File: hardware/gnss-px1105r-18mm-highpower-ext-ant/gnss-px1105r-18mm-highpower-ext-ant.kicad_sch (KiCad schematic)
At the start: 28 parts, among them J4 BM05B-SRSS-TB, J9 2337019-1, U1 PX1105R, U3 TPS62913RPUR

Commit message: hardware: battery protection, boost swap, and a capacitor voltage audit
Base station power chain, all verified against exported netlists:

- Protection: MAX17303G+ gauge/protector and its NTMD6N02R2G FET pair
  replaced by DW01A + 2x FS8205A. The MAX17303 had no firmware driver and
  the board never had a working coulomb counter, so state of charge already
  came from the voltage curve in bs_battery_soc.h; it now reads a 1M/1M
  divider on GPIO1. The FETs move from the positive rail to the negative
  one because the DW01A has no charge pump, so board ground is now P-,
  separated from the cell's B- by the FET stack. Two FS8205A in parallel
  put the 150 mV overcurrent trip at ~4.8-6.0 A instead of ~2.4-3.0 A.
  TH1 moves onto the BQ21040's TS pin, replacing a fixed 10k that had been
  defeating thermal charge cutoff.

- V_LORA retargeted 7.49 V -> 4.95 V and LM5157QRTERQ1 -> TPS61023DRLR.
  Nothing needed 7.4 V (everything downstream is 3.3 V behind the
  TPS62913), while an RFD868x-class radio is 5 V nominal with a 6 V
  absolute maximum, so the old rail put it permanently out of reach. Being
  synchronous and internally compensated also dropped D2, C35-C38 and R10.
  Inductor stays the fleet 2.2 uH: inside TI's 0.37-2.9 uH range and the
  only value meeting their ripple-under-40%-of-average guidance at load.

- Keystone 1043P holder -> MYOUNG BH-18650-A5BJ001-2D. Terminal pitch
  72.30 vs 72.22 mm, so the battery nets did not move; BT2 is rotated 180
  degrees because this part's positive end is mirrored.

Across all four boards:

- Every crystal was mis-loaded. 32.768 kHz parts saw ~9 pF against a 6 pF
  spec and the 40 MHz saw 12.5 pF against 10 pF, both pulling slow. Moved
  to Seiko SC-32S (12.5 pF) with 22 pF load caps, and the 40 MHz caps to
  18 pF. The tolerance being paid for had been swamped several times over.

- Capacitor voltage audit, new Min V rating column in the BOM. Three parts
  were operating outside their rating on 8.4 V rails: 47 uF and 100 u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
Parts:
- J4: footprint CONN_BM05B-SRSS-TB_JST -> Footprints:CONN_BM05B-SRSS-TB_JST
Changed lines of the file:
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@@
 			)
 		)
-		(property "Footprint" "CONN_BM05B-SRSS-TB_JST"
+		(property "Footprint" "Footprints:CONN_BM05B-SRSS-TB_JST"
 			(at 233.045 80.645 0)
 			(hide yes)

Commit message: hardware: declare filled+capped vias on the 6-layer boards; in-progress board edits
Two separate things, kept together because they land in the same board files.

1. Via protection, mine.  lora-daughterboard and rocket-computer both place
   vias in pads, and the fab fills those on 6-layer stackups -- but the board
   files still declared (filling no) (capping no), so nothing in the exported
   data said so.  Both now declare IPC-4761 Type VII (filled and capped),
   which is the process via-in-pad actually requires.  base-station is left at
   (filling no) (capping no): it is 4-layer and does not get the treatment.

2. In-progress layout work, the user's, carried along in the same files:

   rocket-computer  J7 removed (superseded by the J8 JST VH battery inlet);
                    C20/C22/C48/C49 crystal caps 18 pF -> 12 pF now reflected
                    in copper; 8 parts flipped side, 23 repositioned, routing
                    and via count adjusted to suit
   lora-daughterboard  routing and ground stitching (+8 vias, +10 segments)
   base-station     one via removed
   gnss-sam10m8-18mm-hv       C15 added; C11/C13 47 uF -> 22 uF
   gnss-px1105r-...-ext-ant   C16/R8/R9 added; C13/C14 47 uF -> 22 uF

The 47 -> 22 uF swap on both GNSS boards is already reflected in the
cross-board BOM: the 47 uF line is now rocket-computer only (1), and 22 uF
GNSS went 5 -> 8.

Co-Authored-By: Claude Opus 5 <noreply@anthropic.com>
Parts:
- added C16: 22 uF, Capacitor_SMD:C_0805_2012Metric, symbol Device:C
- added R8, R9: 1 k, Resistor_SMD:R_0402_1005Metric, symbol Device:R_US
- C13, C14: value 47 uF -> 22 uF
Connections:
- net GND: now also C16.2
- net GNSS_RX: now also R9.1; no longer J4.1
- net GNSS_TX: now also R8.1; no longer J4.2
- net at C13.1, C14.1, FB1.1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: now also C16.1
- new net: J4.1, R9.2
- new net: J4.2, R8.2

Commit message: hardware: SMF10A TVS on VSYS -- LoRa CR5 and both GNSS boards (schematics)
Closes the LoRa review's finding 12, and extends it to the two GNSS
daughterboards, which turned out to have the same gap in a worse form.

VSYS is fed straight from an externally-handled connector that hot-plugs onto a
live 2S pack, and clamps nothing before the TPS62913's 18 V VIN abs max:

  lora  VSYS = { CR1.1, CR3.1, FL1.1 }   an ORing Schottky damps the ring
  gnss  VSYS = { FL1.1, J.3 }            connector pin straight into the choke

The GNSS boards lack the one element that was damping the LoRa board, so they
sit closer to the limit -- ~14.4 V worst-case ring against ~12.6 V. Neither
breaches 18 V on the hot-plug transient alone; the argument for the part is ESD
on a human-handled connector whose power pin has no protection, while the USB
port beside it does.

Part: PTTC SMF10A, LCSC C5444308, 56k in stock, $0.086 at 50+.
V_RWM 10 V is 19% above the 8.4 V full-charge pack, and V_BR 11.1 V min stays
clear of it even at -40 C. V_C 17 V at 11.8 A sits under the 18 V abs max --
that is what selects this part. The next step up, SMF12A, clamps at 19.9 V,
ABOVE the abs max, so it would pass through the very event being clamped. 10 V
is the only SMF step that clears both ends of this rail's narrow window.

Symbol/footprint/3D were already in the project, unused, from the SS24FL line
that was never fitted -- same SOD-123FL package, pads named A/C. New
Custom:SMF10A reuses Footprints:SODFL3617X108N and 3dmodels/SS24FL.step, with a
zener-style cathode bar so it reads as a unidirectional TVS. Note the existing
SS24FL symbol pointed at "SS24FL:SODFL3617X108N" -- a library nickname this
project never defined -- which is likely why the part was unusable; the new
symbol uses the real "Footprints" nickname.

All three placed at rot 0, the one rotation whose pin transform is verified
against this file. Connectivity confirmed by netlist: cathode on VSYS, anode on
GND, ERC clean on all three boards. P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
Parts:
- added CR1: SMF10A, Footprints:SODFL3617X108N, symbol Custom:SMF10A
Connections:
- net GND: now also CR1.A
- net VSYS: now also CR1.C

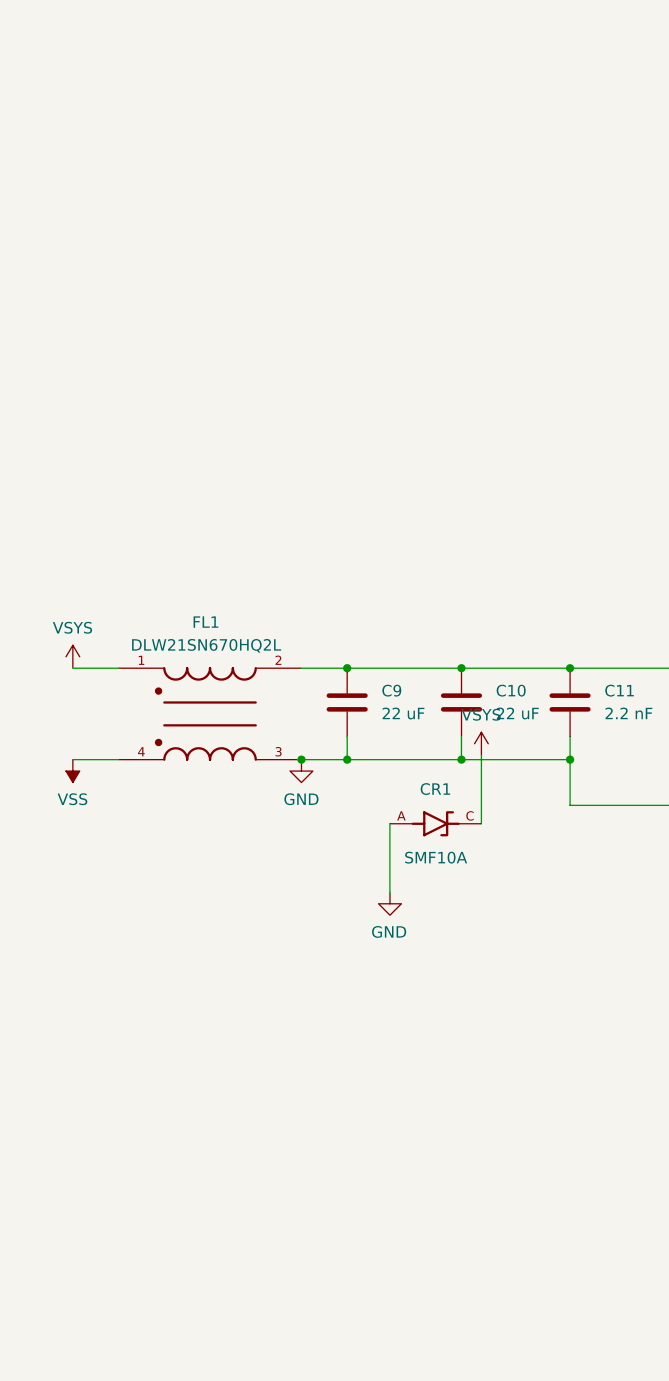
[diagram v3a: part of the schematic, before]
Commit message: hardware: sourcing + BOM-linkage metadata on the SMF10A symbol and all three instances
Library fields do not propagate to already-placed instances, so this writes
both: Custom.kicad_sym for future placements, and CR5 (LoRa) plus CR1 on each
GNSS board for the ones already drawn.

Fields follow the house convention rather than inventing names:

  MPN / Mfr   SMF10A / PTTC   the canonical pair -- what the cross-board BOM
                              audit joins on, and what 406 parts already carry
  Dist        LCSC            mirrors the sheet's own "Dist." column so the two
                              stay diff-checkable, same rationale as the
                              capacitor MinVRating pass
  Dist_PN     C5444308        the orderable key.  Named Dist_PN rather than the
                              LCSC_Part_Number four older symbols use, because
                              sourcing is mixed LCSC/DigiKey/Mouser and the
                              generic name survives a distributor change.
  Description full spec: 10 V standoff, 11.1 V VBR min, 17 V clamp at 11.8 A
                              Ipp, 200 W, SOD-123FL
  Notes       why 10 V and not 12 V -- SMF12A clamps 19.9 V, ABOVE the
                              TPS62913's 18 V VIN abs max, so it is not a
                              substitute despite looking like the same family

Two deliberate omissions. The SnapEDA-inherited MF / MP / MANUFACTURER /
STANDARD / PARTREV / SnapEDA_Link fields are NOT propagated -- that is exactly
where the two stale part numbers cleared in 59d2c67 were hiding, and a second
part-number field is the wrong-part-order hazard this fleet has already been
bitten by. Price is also left out: the BOM is the price authority, and a figure
copied into a symbol goes stale silently with nothing to catch it.

ERC clean on all three boards.

Co-Authored-By: Claude Opus 5 <noreply@anthropic.com>
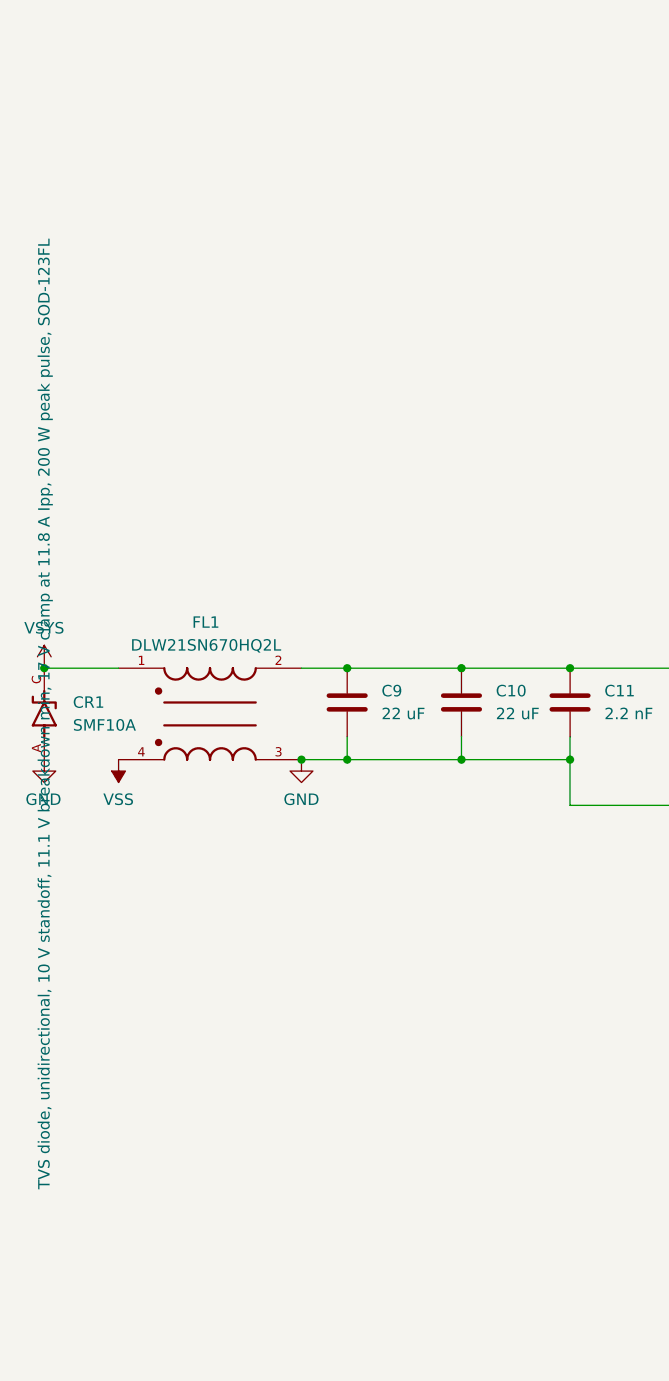
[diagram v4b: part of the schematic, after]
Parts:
- CR1: Dist (none) -> LCSC; Dist_PN (none) -> C5444308; Notes (none) -> Clamp must stay below the TPS62913 VIN abs max of 18 V. SMF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
